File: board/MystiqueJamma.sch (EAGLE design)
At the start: 36 parts, among them IC1 7805, IC2 74LS245N, IC3 74LS245N, IC4 74LS245N, U1 AS6C4008-55PCN

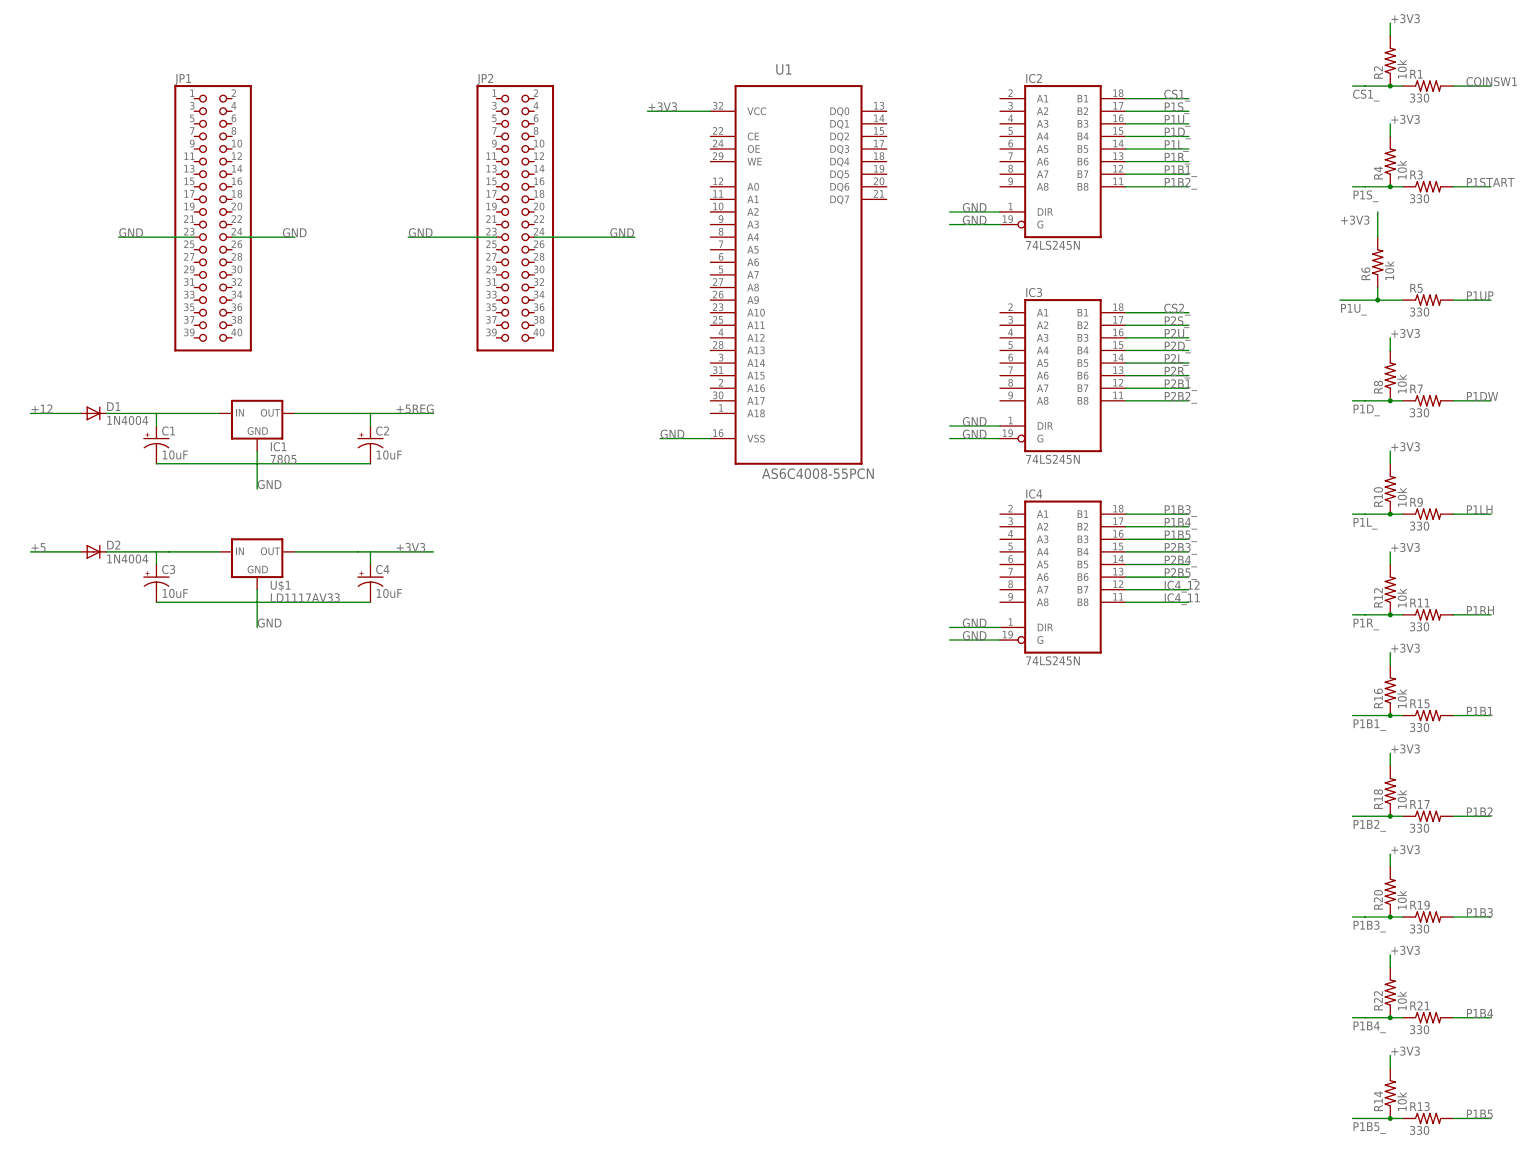
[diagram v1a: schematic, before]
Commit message: included sdcard
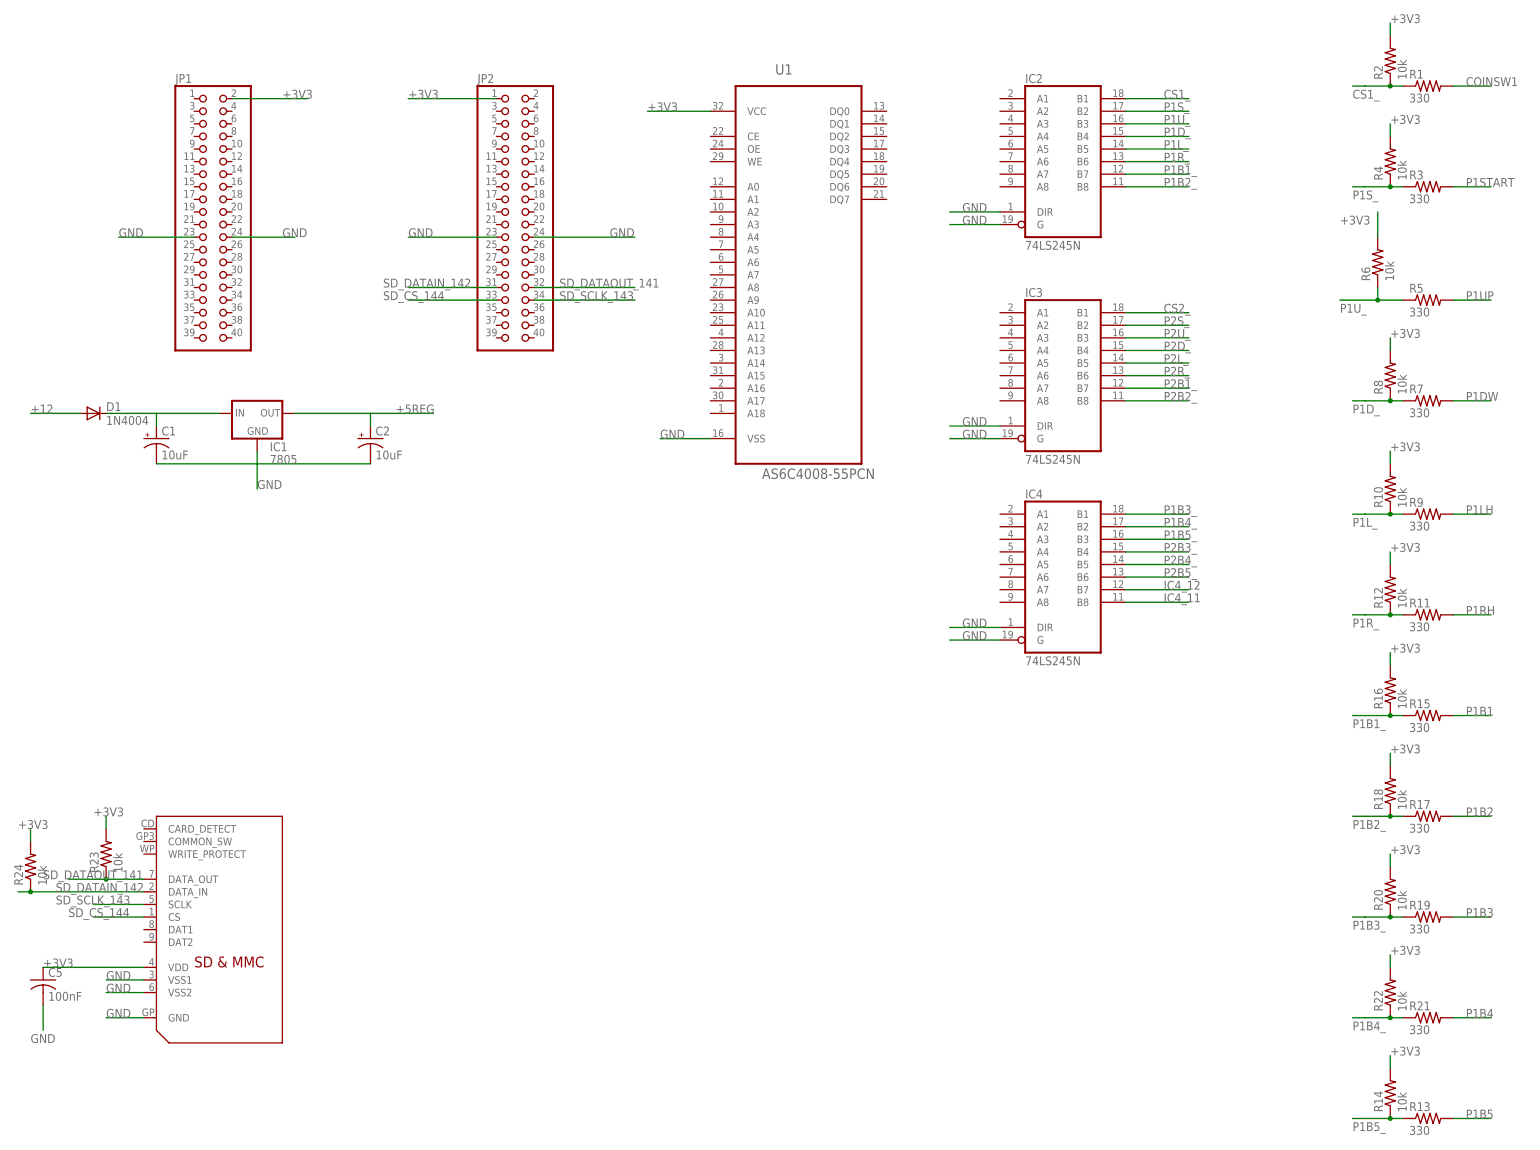
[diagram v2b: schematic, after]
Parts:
- removed C3, C4: 10uF, rcl-2:CPOL-USE2.5-5
- removed D2: 1N4004, adafruit:1N4004
- removed U$1: LD1117AV33, SparkFun-IC-Power:V_REG_78XXSINK
- added C5: 100nF, adafruit:C-US025-024X044
- added R23, R24: 10k, adafruit:R-US_0207/7
- added U$2: SDMMC06132, adafruit:SDMMC06132
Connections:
- removed net +5: D2.A
- removed net N$1: C3.+, D2.C, U$1.IN
- new net SD_CS_144: JP2.33, U$2.CS
- new net SD_DATAIN_142: JP2.31, R24.1, U$2.DATA_IN
- new net SD_DATAOUT_141: JP2.32, R23.1, U$2.DATA_OUT
- new net SD_SCLK_143: JP2.34, U$2.SCLK
- net +3V3: now also C5.1, JP1.2, JP2.1, R23.2, R24.2, U$2.VDD; no longer C4.+, U$1.OUT
- net GND: now also C5.2, U$2.GND, U$2.VSS1, U$2.VSS2; no longer C3.-, C4.-, U$1.GND
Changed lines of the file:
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@@
 <?xml version="1.0" encoding="utf-8"?>
 <!DOCTYPE eagle SYSTEM "eagle.dtd">
-<eagle version="7.5.0">
+<eagle version="9.1.3">
 <drawing>
 <settings>
 <setting alwaysvectorfont="no"/>
+<setting keepoldvectorfont="yes"/>
 <setting verticaltext="up"/>
 </settings>
@@
 <layer number="230" name="230bmp" color="7" fill="1" visible="yes" active="yes"/>
 <layer number="231" name="231bmp" color="7" fill="1" visible="yes" active="yes"/>
+<layer number="232" name="Eagle3D_PG2" color="7" fill="1" visible="no" active="no"/>
+<layer number="233" name="Eagle3D_PG3" color="7" fill="1" visible="no" active="no"/>
 <layer number="248" name="Housing" color="7" fill="1" visible="yes" active="yes"/>
 <layer number="249" name="Edge" color="7" fill="1" visible="yes" active="yes"/>
@@
 <part name="IC3" library="74xx-us" deviceset="74*245" device="N" technology="LS"/>
 <part name="IC4" library="74xx-us" deviceset="74*245" device="N" technology="LS"/>
-<part name="C3" library="rcl-2" deviceset="CPOL-US" device="E2.5-5" value="10uF"/>
-<part name="C4" library="rcl-2" deviceset="CPOL-US" device="E2.5-5" value="10uF"/>
-<part name="U$1" library="SparkFun-IC-Power" deviceset="V_REG_78XX" device="SINK" value="LD1117AV33"/>
 <part name="D1" library="adafruit" deviceset="1N4004" device=""/>
-<part name="D2" library="adafruit" deviceset="1N4004" device=""/>
+<part name="U$2" library="adafruit" deviceset="SDMMC" device="06132"/>
+<part name="R23" library="adafruit" deviceset="R-US_" device="0207/7" value="10k"/>
+<part name="R24" library="adafruit" deviceset="R-US_" device="0207/7" value="10k"/>
+<part name="C5" library="adafruit" deviceset="C-US" device="025-024X044" value="100nF"/>
 </parts>
 <sheets>
@@
 <instance part="IC3" gate="A" x="190.5" y="25.4"/>
 <instance part="IC4" gate="A" x="190.5" y="-15.24"/>
-<instance part="C3" gate="G$1" x="7.62" y="-15.24"/>
-<instance part="C4" gate="G$1" x="50.8" y="-15.24"/>
-<instance part="U$1" gate="G$1" x="27.94" y="-10.16"/>
 <instance part="D1" gate="1" x="-5.08" y="17.78"/>
-<instance part="D2" gate="1" x="-5.08" y="-10.16"/>
+<instance part="U$2" gate="G$1" x="17.78" y="-86.36"/>
+<instance part="R23" gate="G$1" x="-2.54" y="-71.12" rot="R90"/>
+<instance part="R24" gate="G$1" x="-17.78" y="-73.66" rot="R90"/>
+<instance part="C5" gate="G$1" x="-15.24" y="-96.52"/>
 </instances>
 <busses>
@@
 </segment>
 <segment>
-<wire x1="27.94" y1="-17.78" x2="27.94" y2="-20.32" width="0.1524" layer="91"/>
-<label x="27.94" y="-25.4" size="1.778" layer="95"/>
-<pinref part="C3" gate="G$1" pin="-"/>
-<wire x1="27.94" y1="-20.32" x2="27.94" y2="-25.4" width="0.1524" layer="91"/>
-<wire x1="7.62" y1="-20.32" x2="27.94" y2="-20.32" width="0.1524" layer="91"/>
-<pinref part="C4" gate="G$1" pin="-"/>
-<wire x1="27.94" y1="-20.32" x2="50.8" y2="-20.32" width="0.1524" layer="91"/>
-<pinref part="U$1" gate="G$1" pin="GND"/>
+<pinref part="U$2" gate="G$1" pin="GND"/>
+<wire x1="5.08" y1="-104.14" x2="-2.54" y2="-104.14" width="0.1524" layer="91"/>
+<label x="-2.54" y="-104.14" size="1.778" layer="95"/>
+</segment>
+<segment>
+<pinref part="U$2" gate="G$1" pin="VSS2"/>
+<wire x1="5.08" y1="-99.06" x2="-2.54" y2="-99.06" width="0.1524" layer="91"/>
+<label x="-2.54" y="-99.06" size="1.778" layer="95"/>
+</segment>
+<segment>
+<pinref part="U$2" gate="G$1" pin="VSS1"/>
+<wire x1="5.08" y1="-96.52" x2="-2.54" y2="-96.52" width="0.1524" layer="91"/>
+<label x="-2.54" y="-96.52" size="1.778" layer="95"/>
+</segment>
+<segment>
+<pinref part="C5" gate="G$1" pin="2"/>
+<wire x1="-15.24" y1="-101.6" x2="-15.24" y2="-106.68" width="0.1524" layer="91"/>
+<label x="-17.78" y="-109.22" size="1.778" layer="95"/>
 </segment>
 </net>
@@
 </segment>
 <segment>
-<wire x1="35.56" y1="-10.16" x2="48.26" y2="-10.16" width="0.1524" layer="91"/>
-<pinref part="C4" gate="G$1" pin="+"/>
-<wire x1="50.8" y1="-12.7" x2="50.8" y2="-10.16" width="0.1524" layer="91"/>
-<wire x1="50.8" y1="-10.16" x2="48.26" y2="-10.16" width="0.1524" layer="91"/>
-<wire x1="50.8" y1="-10.16" x2="63.5" y2="-10.16" width="0.1524" layer="91"/>
-<label x="55.88" y="-10.16" size="1.778" layer="95"/>
-<pinref part="U$1" gate="G$1" pin="OUT"/>
+<pinref part="R23" gate="G$1" pin="2"/>
+<wire x1="-2.54" y1="-66.04" x2="-2.54" y2="-63.5" width="0.1524" layer="91"/>
+<label x="-5.08" y="-63.5" size="1.778" layer="95"/>
+</segment>
+<segment>
+<pinref part="R24" gate="G$1" pin="2"/>
+<wire x1="-17.78" y1="-68.58" x2="-17.78" y2="-66.04" width="0.1524" layer="91"/>
+<label x="-20.32" y="-66.04" size="1.778" layer="95"/>
+</segment>
+<segment>
+<pinref part="U$2" gate="G$1" pin="VDD"/>
+<wire x1="5.08" y1="-93.98" x2="-15.24" y2="-93.98" width="0.1524" layer="91"/>
+<label x="-15.24" y="-93.98" size="1.778" layer="95"/>
+<pinref part="C5" gate="G$1" pin="1"/>
+</segment>
+<segment>
+<pinref part="JP1" gate="A" pin="2"/>
+<wire x1="22.86" y1="81.28" x2="38.1" y2="81.28" width="0.1524" layer="91"/>
+<label x="33.02" y="81.28" size="1.778" layer="95"/>
+</segment>
+<segment>
+<pinref part="JP2" gate="A" pin="1"/>
+<wire x1="76.2" y1="81.28" x2="58.42" y2="81.28" width="0.1524" layer="91"/>
+<label x="58.42" y="81.28" size="1.778" layer="95"/>
 </segment>
 </net>
@@
 </segment>
 </net>
-<net name="+5" class="0">
-<segment>
-<wire x1="-7.62" y1="-10.16" x2="-17.78" y2="-10.16" width="0.1524" layer="91"/>
-<label x="-17.78" y="-10.16" size="1.778" layer="95"/>
-<pinref part="D2" gate="1" pin="A"/>
-</segment>
-</net>
-<net name="N$1" class="0">
-<segment>
-<pinref part="C3" gate="G$1" pin="+"/>
-<wire x1="7.62" y1="-12.7" x2="7.62" y2="-10.16" width="0.1524" layer="91"/>
-<wire x1="7.62" y1="-10.16" x2="10.16" y2="-10.16" width="0.1524" layer="91"/>
-<pinref part="U$1" gate="G$1" pin="IN"/>
-<wire x1="10.16" y1="-10.16" x2="20.32" y2="-10.16" width="0.1524" layer="91"/>
-<pinref part="D2" gate="1" pin="C"/>
-<wire x1="-2.54" y1="-10.16" x2="7.62" y2="-10.16" width="0.1524" layer="91"/>
-</segment>
-</net>
 <net name="N$2" class="0">
 <segment>
@@
 </segment>
 </net>
+<net name="SD_CS_144" class="0">
+<segment>
+<pinref part="U$2" gate="G$1" pin="CS"/>
+<wire x1="5.08" y1="-83.82" x2="-5.08" y2="-83.82" width="0.1524" layer="91"/>
+<label x="-10.16" y="-83.82" size="1.778" layer="95"/>
+</segment>
+<segment>
+<pinref part="JP2" gate="A" pin="33"/>
+<wire x1="76.2" y1="40.64" x2="58.42" y2="40.64" width="0.1524" layer="91"/>
+<label x="53.34" y="40.64" size="1.778" layer="95"/>
+</segment>
+</net>
+<net name="SD_SCLK_143" class="0">
+<segment>
+<pinref part="U$2" gate="G$1" pin="SCLK"/>
+<wire x1="5.08" y1="-81.28" x2="-5.08" y2="-81.28" width="0.1524" layer="91"/>
+<label x="-12.7" y="-81.28" size="1.778" layer="95"/>
+</segment>
+<segment>
+<pinref part="JP2" gate="A" pin="34"/>
+<wire x1="83.82" y1="40.64" x2="104.14" y2="40.64" width="0.1524" layer="91"/>
+<label x="88.9" y="40.64" size="1.778" layer="95"/>
+</segment>
+</net>
+<net name="SD_DATAIN_142" class="0">
+<segment>
+<pinref part="U$2" gate="G$1" pin="DATA_IN"/>
+<wire x1="5.08" y1="-78.74" x2="-17.78" y2="-78.74" width="0.1524" layer="91"/>
+<label x="-12.7" y="-78.74" size="1.778" layer="95"/>
+<pinref part="R24" gate="G$1" pin="1"/>
+<wire x1="-17.78" y1="-78.74" x2="-20.32" y2="-78.74" width="0.1524" layer="91"/>
+<junction x="-17.78" y="-78.74"/>
+</segment>
+<segment>
+<pinref part="JP2" gate="A" pin="31"/>
+<wire x1="76.2" y1="43.18" x2="58.42" y2="43.18" width="0.1524" layer="91"/>
+<label x="53.34" y="43.18" size="1.778" layer="95"/>
+</segment>
+</net>
+<net name="SD_DATAOUT_141" class="0">
+<segment>
+<pinref part="U$2" gate="G$1" pin="DATA_OUT"/>
+<wire x1="5.08" y1="-76.2" x2="-2.54" y2="-76.2" width="0.1524" layer="91"/>
+<label x="-15.24" y="-76.2" size="1.778" layer="95"/>
+<pinref part="R23" gate="G$1" pin="1"/>
+<wire x1="-2.54" y1="-76.2" x2="-10.16" y2="-76.2" width="0.1524" layer="91"/>
+<junction x="-2.54" y="-76.2"/>
+</segment>
+<segment>
+<pinref part="JP2" gate="A" pin="32"/>
+<wire x1="83.82" y1="43.18" x2="104.14" y2="43.18" width="0.1524" layer="91"/>
+<label x="88.9" y="43.18" size="1.778" layer="95"/>
+</segment>
+</net>
